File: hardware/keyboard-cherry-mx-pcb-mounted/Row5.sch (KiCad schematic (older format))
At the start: 14 parts, among them SW30 Ctrl, SW32 Workspace, SW34 Alt, SW36 Space, SW38 Left Arrow, SW40 Down Arrow, SW42 Right Arrow

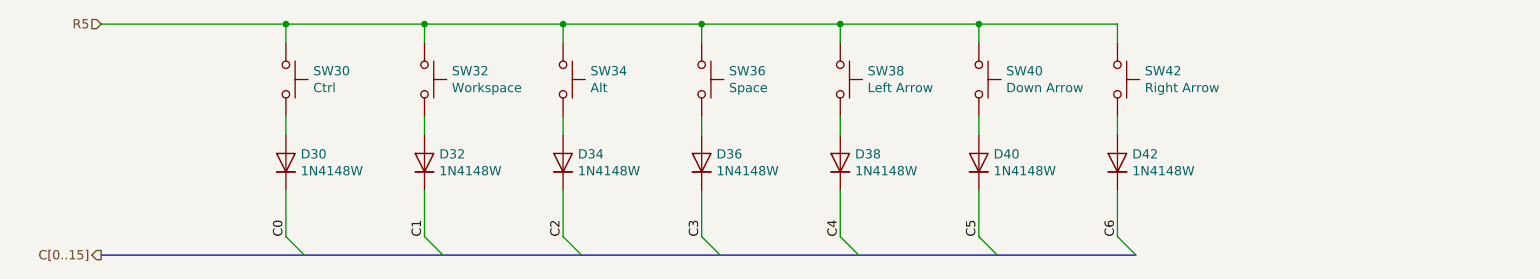
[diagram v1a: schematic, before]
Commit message: Adds completed sensor and power connections. Still need to add USB footprint then sch are done for version 1.0
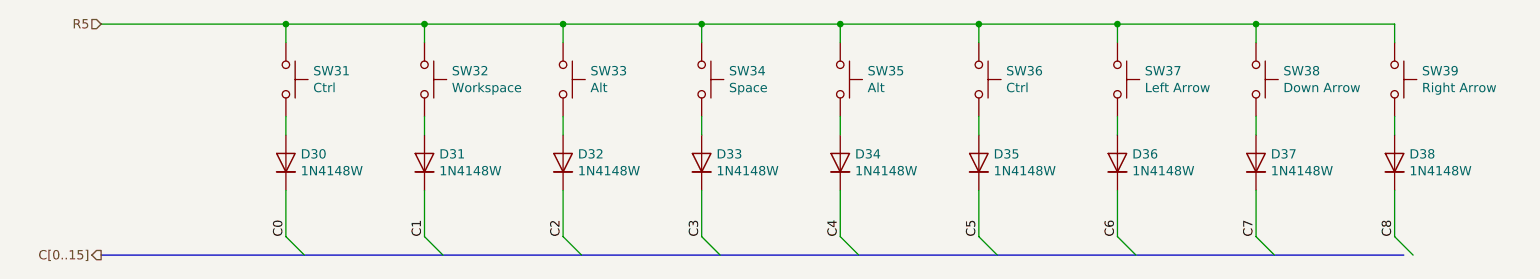
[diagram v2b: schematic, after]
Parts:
- added D34, D35: 1N4148W, Diode_SMD:D_SOD-123, symbol Diode:1N4148W
- added SW35: Alt, Button_Switch_Keyboard:SW_Cherry_MX_1.50u_PCB, symbol Switch:SW_Push
- added SW36: Ctrl, Button_Switch_Keyboard:SW_Cherry_MX_1.50u_PCB, symbol Switch:SW_Push
- renumbered D32 to D31, D34 to D32, D36 to D33, D38 to D36, D40 to D37, D42 to D38, SW30 to SW31, SW34 to SW33, SW36 to SW34, SW38 to SW37, SW40 to SW38, SW42 to SW39
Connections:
- net C4: now also D34.1 (K); no longer D36.1 (K)
- net C5: now also D35.1 (K); no longer D37.1 (K)
- net C6: now also D36.1 (K); no longer D38.1 (K)
- net R5: now also SW35.1, SW36.1
- new net: D34.2 (A), SW35.2
- new net: D35.2 (A), SW36.2
- new net C7: D37.1 (K)
- new net C8: D38.1 (K)
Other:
- moved on the sheet: D36, D37, D38, SW37, SW38, SW39

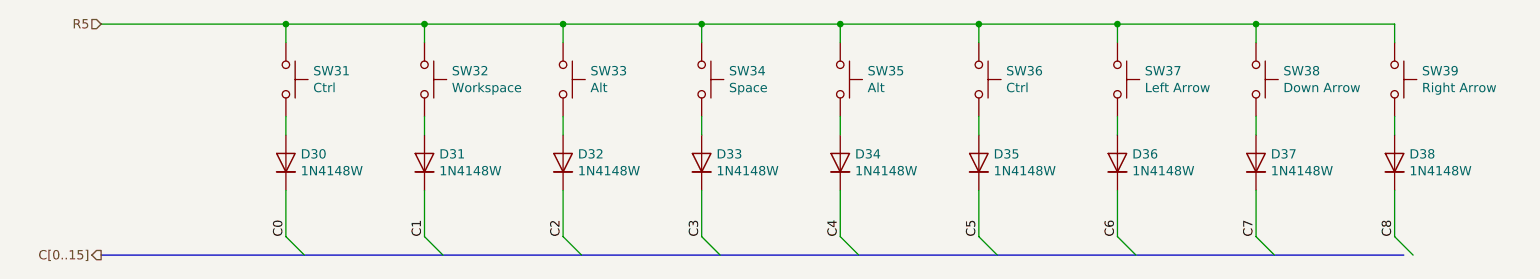
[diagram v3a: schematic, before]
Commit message: Aligns the keys so the column connections are more consistent. e.g. right most keys will have same column connection.
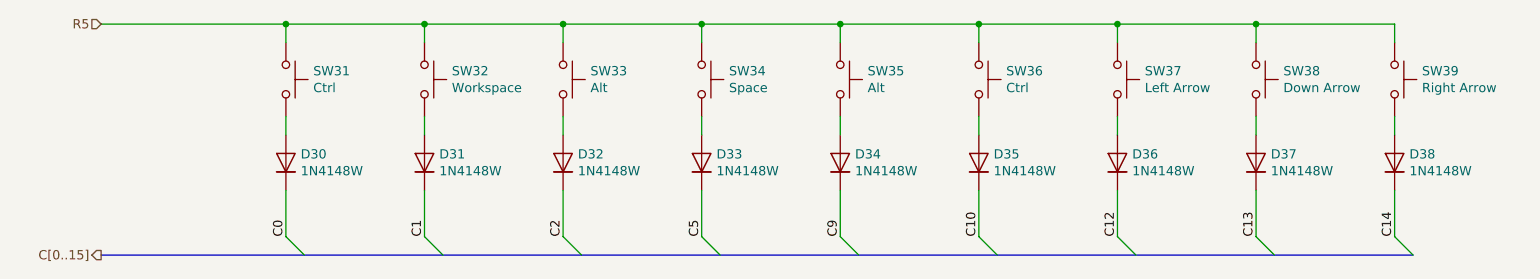
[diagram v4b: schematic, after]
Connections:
- net C3 is gone; now on net C5: D33.1 (K)
- net C5: no longer D35.1 (K)
- net C4 renamed C9
- net C6 renamed C12
- net C7 renamed C13
- net C8 renamed C14
- new net C10: D35.1 (K)
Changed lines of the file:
@@
 C2
 Text Label 5400 3250 1    50   ~ 0
-C3
+C5
 Text Label 7650 3250 1    50   ~ 0
-C6
+C12
 Text Label 8400 3250 1    50   ~ 0
-C7
+C13
 Text Label 9150 3250 1    50   ~ 0
-C8
+C14
 Entry Wire Line
 	3150 3250 3250 3350
@@
 	6900 3000 6900 3250
 Text Label 6150 3250 1    50   ~ 0
-C4
+C9
 Text Label 6900 3250 1    50   ~ 0
-C5
+C10
 Entry Wire Line
 	6150 3250 6250 3350
@@
 	6150 2100 6900 2100
 Wire Bus Line
-	2150 3350 9200 3350
+	2150 3350 9250 3350
 $EndSCHEMATC

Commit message: Adds labels for each key and creates gerber files.
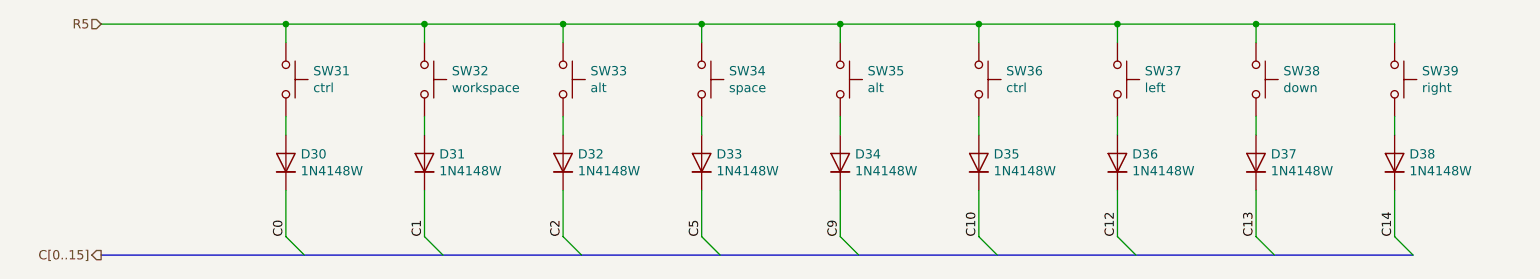
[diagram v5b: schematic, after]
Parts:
- SW31, SW36: value Ctrl -> ctrl
- SW32: value Workspace -> workspace
- SW33, SW35: value Alt -> alt
- SW34: value Space -> space
- SW37: value Left Arrow -> left
- SW38: value Down Arrow -> down
- SW39: value Right Arrow -> right
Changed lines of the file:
@@
 AR Path="/5E697948/5E78F98F/5E77EF80" Ref="SW31"  Part="1"
 F 0 "SW31" V 3104 2548 50  0000 L CNN
-F 1 "Ctrl" V 3195 2548 50  0000 L CNN
+F 1 "ctrl" V 3195 2548 50  0000 L CNN
 F 2 "Button_Switch_Keyboard:SW_Cherry_MX_1.25u_PCB" H 3150 2600 50  0001 C CNN
 F 3 "~" H 3150 2600 50  0001 C CNN
@@
 AR Path="/5E697948/5E78F98F/5E818F10" Ref="SW32"  Part="1"
 F 0 "SW32" V 3854 2548 50  0000 L CNN
-F 1 "Workspace" V 3945 2548 50  0000 L CNN
+F 1 "workspace" V 3945 2548 50  0000 L CNN
 F 2 "Button_Switch_Keyboard:SW_Cherry_MX_1.25u_PCB" H 3900 2600 50  0001 C CNN
 F 3 "~" H 3900 2600 50  0001 C CNN
@@
 AR Path="/5E697948/5E78F98F/5E77EF9E" Ref="SW33"  Part="1"
 F 0 "SW33" V 4604 2548 50  0000 L CNN
-F 1 "Alt" V 4695 2548 50  0000 L CNN
+F 1 "alt" V 4695 2548 50  0000 L CNN
 F 2 "Button_Switch_Keyboard:SW_Cherry_MX_1.25u_PCB" H 4650 2600 50  0001 C CNN
 F 3 "~" H 4650 2600 50  0001 C CNN
@@
 AR Path="/5E697948/5E78F98F/5E77EFAC" Ref="SW34"  Part="1"
 F 0 "SW34" V 5354 2548 50  0000 L CNN
-F 1 "Space" V 5445 2548 50  0000 L CNN
+F 1 "space" V 5445 2548 50  0000 L CNN
 F 2 "Button_Switch_Keyboard:SW_Cherry_MX_6.25u_PCB" H 5400 2600 50  0001 C CNN
 F 3 "~" H 5400 2600 50  0001 C CNN
@@
 AR Path="/5E697948/5E78F98F/5E818F16" Ref="SW37"  Part="1"
 F 0 "SW37" V 7604 2548 50  0000 L CNN
-F 1 "Left Arrow" V 7695 2548 50  0000 L CNN
+F 1 "left" V 7695 2548 50  0000 L CNN
 F 2 "Button_Switch_Keyboard:SW_Cherry_MX_1.00u_PCB" H 7650 2600 50  0001 C CNN
 F 3 "~" H 7650 2600 50  0001 C CNN
@@
 AR Path="/5E697948/5E78F98F/5E818F18" Ref="SW38"  Part="1"
 F 0 "SW38" V 8354 2548 50  0000 L CNN
-F 1 "Down Arrow" V 8445 2548 50  0000 L CNN
+F 1 "down" V 8445 2548 50  0000 L CNN
 F 2 "Button_Switch_Keyboard:SW_Cherry_MX_1.00u_PCB" H 8400 2600 50  0001 C CNN
 F 3 "~" H 8400 2600 50  0001 C CNN
@@
 AR Path="/5E697948/5E78F98F/5E77EFD6" Ref="SW39"  Part="1"
 F 0 "SW39" V 9104 2548 50  0000 L CNN
-F 1 "Right Arrow" V 9195 2548 50  0000 L CNN
+F 1 "right" V 9195 2548 50  0000 L CNN
 F 2 "Button_Switch_Keyboard:SW_Cherry_MX_1.00u_PCB" H 9150 2600 50  0001 C CNN
 F 3 "~" H 9150 2600 50  0001 C CNN
@@
 AR Path="/5E697948/5E78F98F/5EA3F324" Ref="SW35"  Part="1"
 F 0 "SW35" V 6104 2548 50  0000 L CNN
-F 1 "Alt" V 6195 2548 50  0000 L CNN
+F 1 "alt" V 6195 2548 50  0000 L CNN
 F 2 "Button_Switch_Keyboard:SW_Cherry_MX_1.50u_PCB" H 6150 2600 50  0001 C CNN
 F 3 "~" H 6150 2600 50  0001 C CNN
@@
 AR Path="/5E697948/5E78F98F/5EA3F332" Ref="SW36"  Part="1"
 F 0 "SW36" V 6854 2548 50  0000 L CNN
-F 1 "Ctrl" V 6945 2548 50  0000 L CNN
+F 1 "ctrl" V 6945 2548 50  0000 L CNN
 F 2 "Button_Switch_Keyboard:SW_Cherry_MX_1.50u_PCB" H 6900 2600 50  0001 C CNN
 F 3 "~" H 6900 2600 50  0001 C CNN
